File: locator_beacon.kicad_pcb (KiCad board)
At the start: 2 copper layers, 44.2 x 19.9 mm, 37 parts, among them Q1 IRLZ44N, U3 L78L05_SOT89, U5 TL074

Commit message: Add boost IC
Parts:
- removed D1: S1M, Diode_SMD:D_SMA
- removed Q1: IRLZ44N, Package_TO_SOT_SMD:SOT-89-3_Handsoldering
- removed REF**: KiCad-Logo2_5mm_SilkScreen, Symbol:KiCad-Logo2_5mm_SilkScreen
- removed REF**: OSHW-Symbol_6.7x6mm_SilkScreen, Symbol:OSHW-Symbol_6.7x6mm_SilkScreen
- added C3: 4.7u, Capacitor_SMD:C_1206_3216Metric_Pad1.33x1.80mm_HandSolder, F.Cu at (134.6, 77.2)
- added D3: B120-E3, Diode_SMD:D_SMA_Handsoldering, F.Cu at (136.4, 72.9)
- added U4: ~, Package_TO_SOT_SMD:SOT-23-5_HandSoldering, F.Cu at (129.3, 71.1)
- C1: value C_Polarized -> 4.7uF
- C4: value 150u -> 2.2u; footprint Capacitor_THT:CP_Radial_D4.0mm_P1.50mm -> Capacitor_SMD:C_1206_3216Metric_Pad1.33x1.80mm_HandSolder; moved to F.Cu
- C8: moved to F.Cu
- L1: value 22u -> 10u
- R16: value 100k -> 230k
- moved R16 9.98 mm to (139.9, 69.6)
- moved R15 9.93 mm to (134.8, 69.6)
- moved C4 6.41 mm to (125.5, 71.1), turned to 90 degrees
- moved C8 5.62 mm to (140.7, 76.8), turned to 0 degrees
- moved D2 3.42 mm to (137.0, 77.2), turned to -90 degrees
- moved C2 0.97 mm to (119.6, 76.7), turned to 180 degrees
- moved C1 0.16 mm to (158.8, 66.7)
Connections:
- R15 pad 1: /power/Vsense -> Net-(U4-FB)
- R16 pad 1: /power/Vsense -> Net-(U4-FB)
- U1 pad 16: /power/PWMctl -> unconnected-(U1-GP0-Pad16)
- U1 pad 4: /power/Vsense -> unconnected-(U1-GP29-Pad4)
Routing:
- net /power/PWMctl: track 16.6 -> 0.00 mm
- net Net-(U4-FB): track 0.00 -> 8.87 mm
- net GND: track 104.0 -> 110.2 mm
- net /power/Vsense: track 4.91 -> 0.00 mm
- net Net-(D3-A): track 12.1 -> 7.89 mm
- net +BATT: track 17.8 -> 20.2 mm
- net Vdrive: track 48.0 -> 48.6 mm, vias 2 -> 1

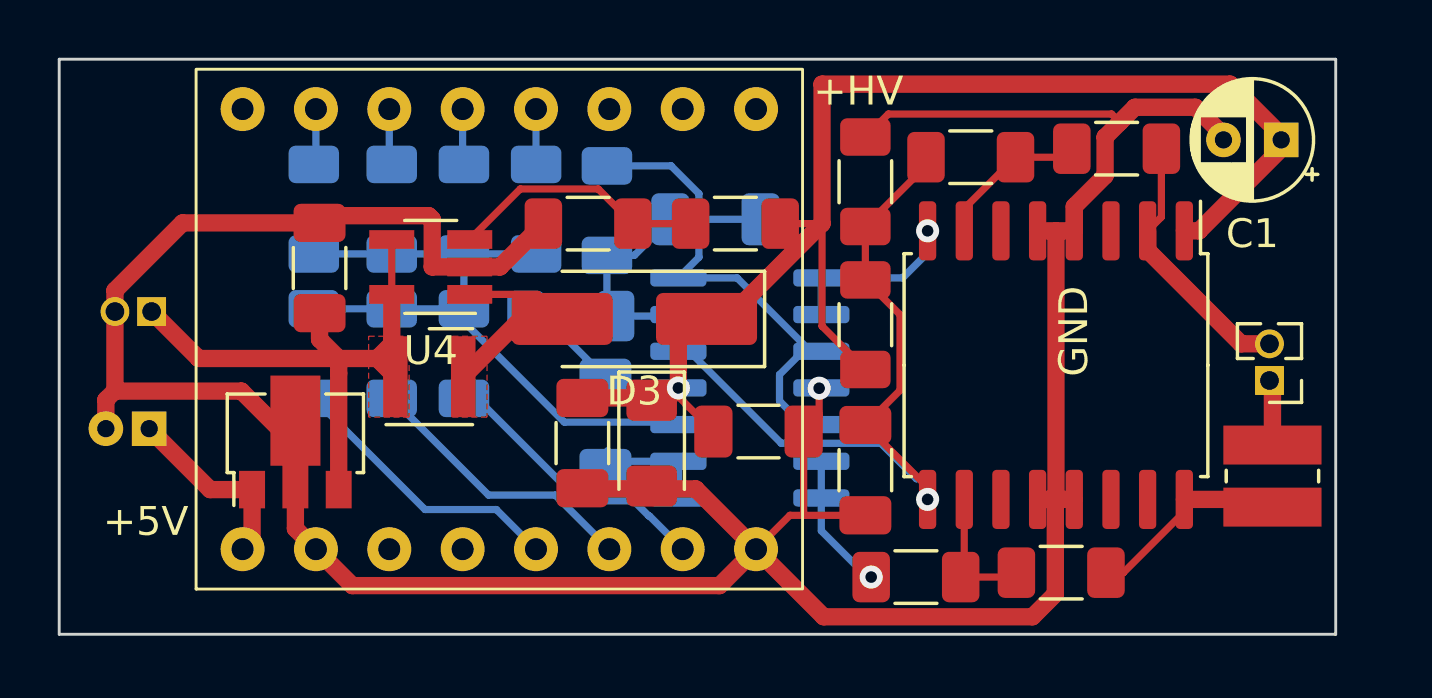
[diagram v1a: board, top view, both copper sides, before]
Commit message: First production prototype
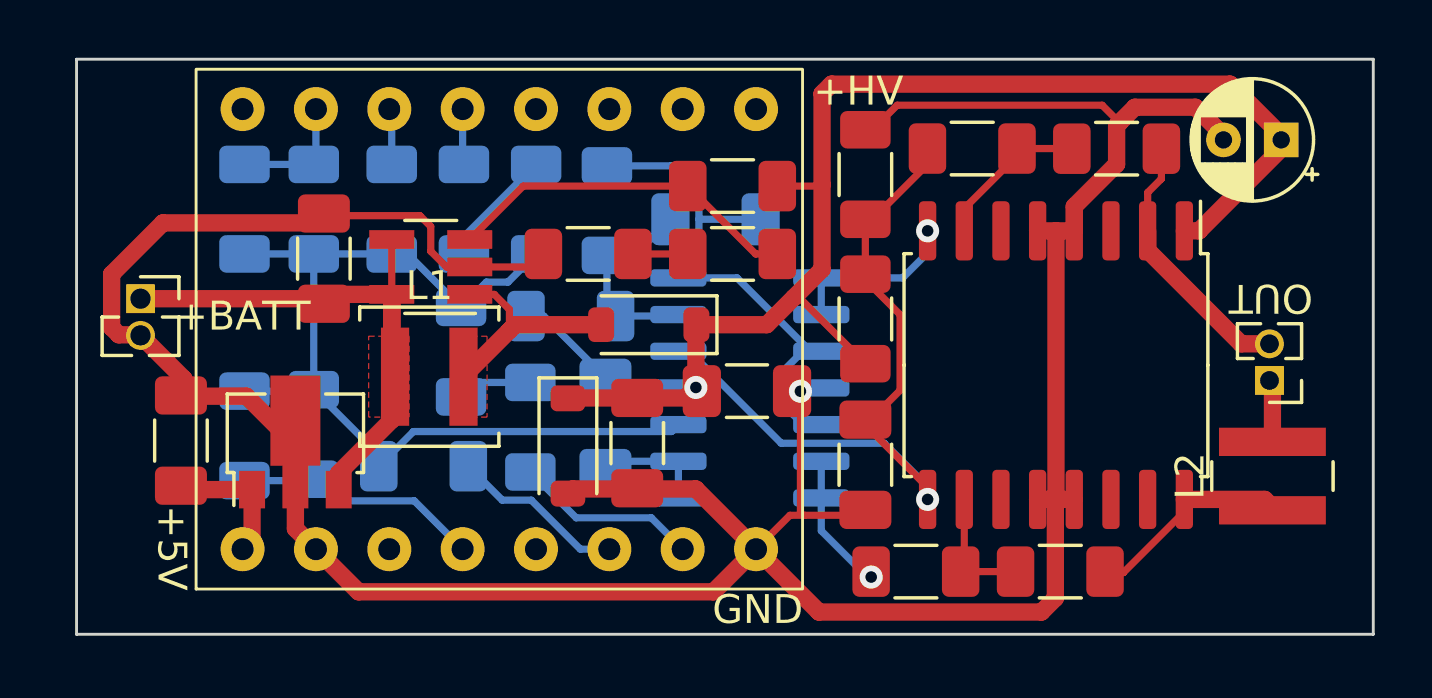
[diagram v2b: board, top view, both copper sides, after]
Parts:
- removed C4: 2.2u, Capacitor_SMD:C_1206_3216Metric_Pad1.33x1.80mm_HandSolder
- added C5: 4.7u, Capacitor_SMD:C_1206_3216Metric_Pad1.33x1.80mm_HandSolder, F.Cu at (120.7, 77.1)
- added R12: 2k, Resistor_SMD:R_1206_3216Metric_Pad1.30x1.75mm_HandSolder, B.Cu at (122.9, 69.1)
- added R13: 16k, Resistor_SMD:R_1206_3216Metric_Pad1.30x1.75mm_HandSolder, B.Cu at (122.9, 77.0)
- added R17: 16k, Resistor_SMD:R_1206_3216Metric_Pad1.30x1.75mm_HandSolder, B.Cu at (130.4, 74.0)
- added R18: 2k, Resistor_SMD:R_1206_3216Metric_Pad1.30x1.75mm_HandSolder, F.Cu at (134.8, 70.7)
- BT1: footprint Connector_PinHeader_1.27mm:PinHeader_1x02_P1.27mm_Vertical -> Connector_PinSocket_1.27mm:PinSocket_1x02_P1.27mm_Vertical; moved to F.Cu
- C1: value 4.7uF -> 4.7u
- C2: value 150u -> 4.7u; footprint Capacitor_THT:CP_Radial_D4.0mm_P1.50mm -> Capacitor_SMD:C_1206_3216Metric_Pad1.33x1.80mm_HandSolder; moved to F.Cu
- C8: value 10n -> 10u
- D2: footprint Diode_SMD:D_1206_3216Metric_Pad1.42x1.75mm_HandSolder -> Diode_SMD:D_SOD-123
- D3: footprint Diode_SMD:D_SMA_Handsoldering -> Diode_SMD:D_SOD-123
- L1: footprint Inductor_SMD_Wurth:L_Wurth_WE-LQSH-3012 -> Inductor_SMD:L_Coilcraft_XAL4030-XXX
- L2: footprint Inductor_SMD:L_Wuerth_MAPI-3020 -> Inductor_SMD:L_Wuerth_MAPI-4030
- R10: value 1k -> 2k
- R11: value 64k -> 16k
- R15: value 10k -> 2k
- R16: value 230k -> 100k
- R20: value 18.8k -> 16k
- R4: value 13.4k -> 16k
- R5: value 32k -> 16k
- R7: value 8k -> 2k
- R8: value 4k -> 2k
- U2: value ~ -> TCA0372
- U4: value ~ -> MIC2288
- moved C2 8.44 mm to (125.7, 70.8), turned to 90 degrees
- moved R15 5.11 mm to (139.8, 70.7)
- moved R5 4.05 mm to (129.1, 78.0), turned to 0 degrees
- moved R11 3.43 mm to (132.8, 76.7)
- moved D2 2.90 mm to (134.1, 77.3)
- moved R6 2.80 mm to (125.3, 76.9)
- moved C3 1.90 mm to (136.5, 77.2)
- moved C8 1.46 mm to (140.3, 75.4)
- moved R16 1.30 mm to (139.8, 68.3)
- moved BT1 0.59 mm to (119.3, 72.2), turned to 0 degrees
- moved D3 0.54 mm to (136.9, 73.1)
- moved R21 0.30 mm to (148.1, 67.0)
- moved R19 0.25 mm to (144.4, 67.9)
- moved R2 0.20 mm to (144.4, 72.9)
- moved R3 0.19 mm to (146.2, 81.7)
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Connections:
- C2 pad 1: +5V -> +BATT
- R11 pad 1: Net-(U5A-+) -> Net-(R11-Pad1)
- R15 pad 2: GND -> Net-(R15-Pad2)
- R6 pad 2: Net-(U1-GP28) -> Net-(U1-GP29)
- R7 pad 1: Net-(U1-GP4) -> Net-(U5A-+)
- R7 pad 2: Net-(U5A-+) -> Net-(R7-Pad2)
- R8 pad 2: Net-(U5A-+) -> Net-(R7-Pad2)
- U1 pad 12: Net-(U1-GP4) -> unconnected-(U1-GP4-Pad12)
- U1 pad 4: unconnected-(U1-GP29-Pad4) -> Net-(U1-GP29)
- U1 pad 5: Net-(U1-GP28) -> unconnected-(U1-GP28-Pad5)
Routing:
- net Net-(U1-GP28): track 9.86 -> 0.00 mm
- net Net-(U5A-+): track 24.1 -> 33.3 mm
- net Net-(U1-GP29): track 0.00 -> 8.58 mm
- net Net-(R7-Pad2): track 0.00 -> 4.14 mm
- net Vdrive: track 48.6 -> 44.8 mm
- net Net-(U1-GP27): track 9.70 -> 6.07 mm
- net Net-(U4-FB): track 8.87 -> 12.4 mm
- net Net-(U1-GP26): track 9.74 -> 6.38 mm
- net Net-(R11-Pad1): track 0.00 -> 2.61 mm
- net Net-(U1-GP1): track 2.05 -> 4.34 mm
- net +5V: track 6.64 -> 4.61 mm
- net Net-(U1-GP4): track 1.92 -> 0.00 mm
- net Net-(R15-Pad2): track 0.00 -> 1.90 mm
- net +BATT: track 20.2 -> 21.8 mm
- net GND: track 110.2 -> 109.6 mm
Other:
- board size 44.2 x 19.9 mm -> 44.9 x 19.9 mm
- board text added: "DAC"
- board text added: "OUT"
- board text added: "SHAPER"

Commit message: Prod 1a
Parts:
- BT1: footprint Connector_PinSocket_1.27mm:PinSocket_1x02_P1.27mm_Vertical -> Connector_PinHeader_2.54mm:PinHeader_1x02_P2.54mm_Vertical
- OUT1: footprint Connector_PinHeader_1.27mm:PinHeader_1x02_P1.27mm_Vertical -> Connector_PinSocket_2.54mm:PinSocket_1x02_P2.54mm_Vertical
- U3: footprint Package_TO_SOT_SMD:SOT-89-3 -> Package_TO_SOT_SMD:TO-252-2
- moved R19 9.89 mm to (143.1, 77.7), turned to 0 degrees
- moved BT1 7.21 mm to (119.3, 79.4)
- moved C5 6.70 mm to (127.4, 77.2), turned to -90 degrees
- moved U3 5.81 mm to (122.6, 71.4)
- moved C6 4.60 mm to (144.4, 73.3)
- moved R2 4.55 mm to (144.4, 68.3), turned to 90 degrees
- moved U4 2.53 mm to (131.3, 69.5)
- moved C2 2.25 mm to (127.3, 69.3)
- moved R18 1.80 mm to (136.1, 69.4), turned to -90 degrees
- moved L1 1.70 mm to (130.9, 74.5)
- moved D2 0.40 mm to (134.5, 77.3)
- moved C3 0.35 mm to (136.8, 77.2)
- moved C8 0.35 mm to (140.7, 75.4)
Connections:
- U3 pad 1: +5V -> +BATT
- U3 pad 3: +BATT -> +5V
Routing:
- net GND: track 109.6 -> 95.2 mm
- net +5V: track 4.61 -> 7.86 mm
- net Net-(U4-FB): track 12.4 -> 9.93 mm
- net Vdrive: track 44.8 -> 42.5 mm
- net /VGND: track 25.6 -> 26.9 mm
- net Net-(D3-A): track 7.99 -> 7.05 mm
- net Net-(OUT1-Pad2): track 8.98 -> 8.46 mm
- removed copper zone on F.Cu, net +BATT
- removed copper zone on F.Cu, net Net-(D3-A)
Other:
- board text added: "BOOST"

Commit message: Forgot to save
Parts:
- removed C8: 10u, Capacitor_SMD:C_1206_3216Metric_Pad1.33x1.80mm_HandSolder
- removed D2: 30V, Diode_SMD:D_SOD-123
- removed R10, R7, R8, R9: 2k, Resistor_SMD:R_1206_3216Metric_Pad1.30x1.75mm_HandSolder
- removed R11, R13, R17, R20, R4, R5, R6: 16k, Resistor_SMD:R_1206_3216Metric_Pad1.30x1.75mm_HandSolder
- removed U3: L78L05_SOT89, Package_TO_SOT_SMD:TO-252-2
- removed U5: TL074, Package_SO:SOIC-14_3.9x8.7mm_P1.27mm
- added C4: 4.7u, Capacitor_SMD:C_1206_3216Metric_Pad1.33x1.80mm_HandSolder, F.Cu at (126.3, 54.7)
- added L3: 4.7u, Inductor_SMD:L_Coilcraft_XAL4030-XXX, F.Cu at (126.2, 59.4)
- added U6: XC9140, Package_SO:TSOP-5_1.65x3.05mm_P0.95mm, F.Cu at (131.5, 58.7)
- C5: value 4.7u -> 10u
- C6, R1, R14, R19, R2, R21, R3, U2: moved to B.Cu
- C7: value 2.2n -> 4.7n
- moved R1 16.3 mm to (146.9, 65.9)
- moved L2 16.2 mm to (174.7, 76.8)
- moved R14 16.2 mm to (141.2, 78.0)
- moved R21 11.1 mm to (139.7, 74.2), turned to -90 degrees
- moved R12 9.48 mm to (132.3, 69.8)
- moved R3 9.42 mm to (142.3, 73.0), turned to -90 degrees
- moved R19 8.26 mm to (134.9, 76.3), turned to 90 degrees
- moved C6 7.71 mm to (137.3, 76.3)
- moved R2 7.34 mm to (137.2, 69.8)
- moved C7 4.43 mm to (134.8, 69.8), turned to 90 degrees
- moved C9 2.90 mm to (132.5, 76.4)
- moved OUT1 2.86 mm to (157.9, 72.2), turned to 0 degrees
- moved U2 2.26 mm to (149.2, 73.2), turned to 90 degrees
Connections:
- C7 pad 1: Net-(U5B--) -> Net-(C7-Pad1)
- C7 pad 2: Net-(U5C-+) -> Net-(U2A-+)
- C9 pad 1: Net-(C9-Pad1) -> Net-(C7-Pad1)
- C9 pad 2: Net-(U5A--) -> GND
- R12 pad 2: Net-(U5A-+) -> Net-(C7-Pad1)
- R3 pad 2: Net-(U5D--) -> Net-(U2A-+)
- U1 pad 13: Net-(U1-GP3) -> unconnected-(U1-GP3-Pad13)
- U1 pad 14: Net-(U1-GP2) -> unconnected-(U1-GP2-Pad14)
- U1 pad 3: +3.3V -> unconnected-(U1-3V3-Pad3)
- U1 pad 4: Net-(U1-GP29) -> unconnected-(U1-GP29-Pad4)
- U1 pad 6: Net-(U1-GP27) -> unconnected-(U1-GP27-Pad6)
- U1 pad 7: Net-(U1-GP26) -> unconnected-(U1-GP26-Pad7)
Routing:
- net Vdrive: track 42.5 -> 0.00 mm, vias 1 -> 0
- net GND: track 95.2 -> 55.2 mm, vias 1 -> 0
- net Net-(U5A-+): track 33.3 -> 0.00 mm
- net Net-(U5C-+): track 19.0 -> 0.00 mm
- net /VGND: track 26.9 -> 16.4 mm, vias 1 -> 0
- net Net-(OUT1-Pad2): track 8.46 -> 18.1 mm
- net Net-(U1-GP29): track 8.58 -> 0.00 mm
- net Net-(U2A--): track 5.06 -> 13.4 mm
- net Net-(U5B--): track 7.14 -> 0.00 mm
- net Net-(U1-GP26): track 6.38 -> 0.00 mm
- net Net-(U1-GP27): track 6.07 -> 0.00 mm
- net Net-(C7-Pad1): track 0.00 -> 5.93 mm
- net Net-(U2B--): track 4.27 -> 9.91 mm
- net Net-(U5D--): track 4.84 -> 0.00 mm, vias 1 -> 0
- net Net-(U1-GP1): track 4.34 -> 0.00 mm
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
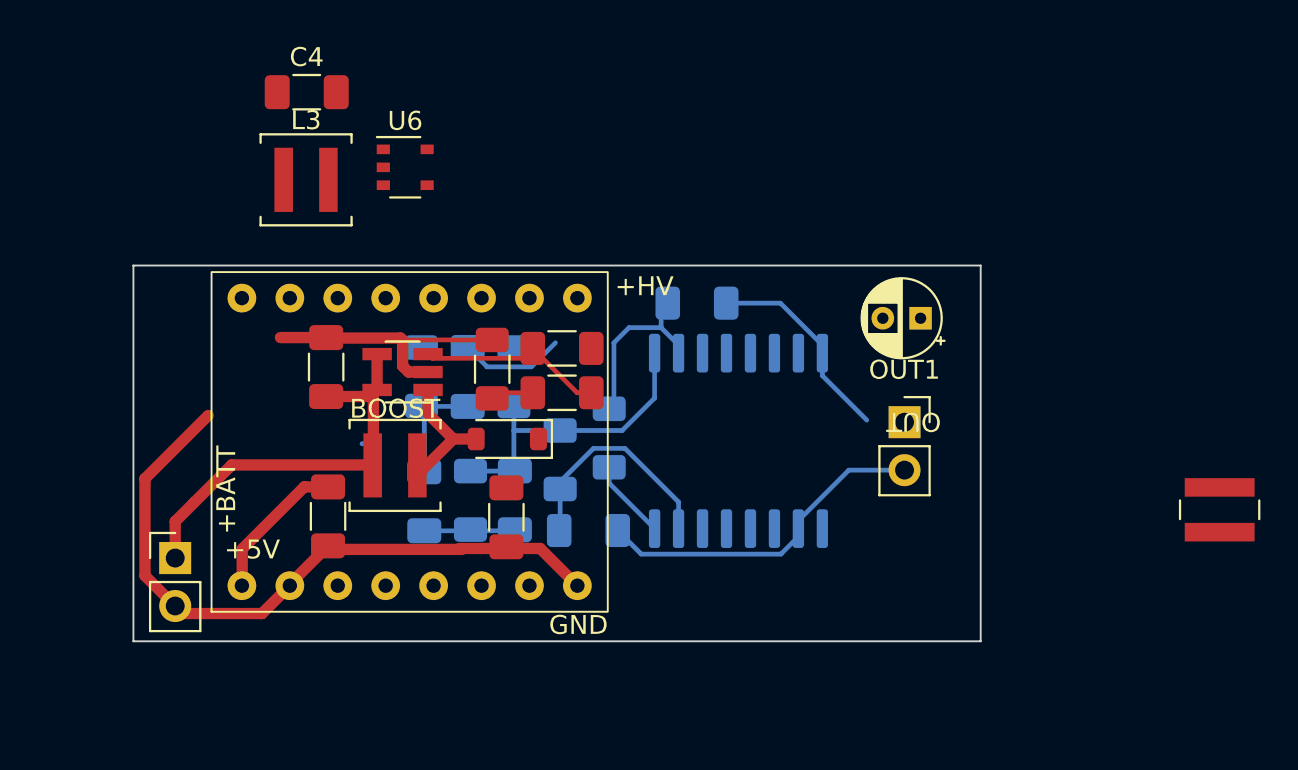
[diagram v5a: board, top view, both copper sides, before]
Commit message: Basic Class D amp
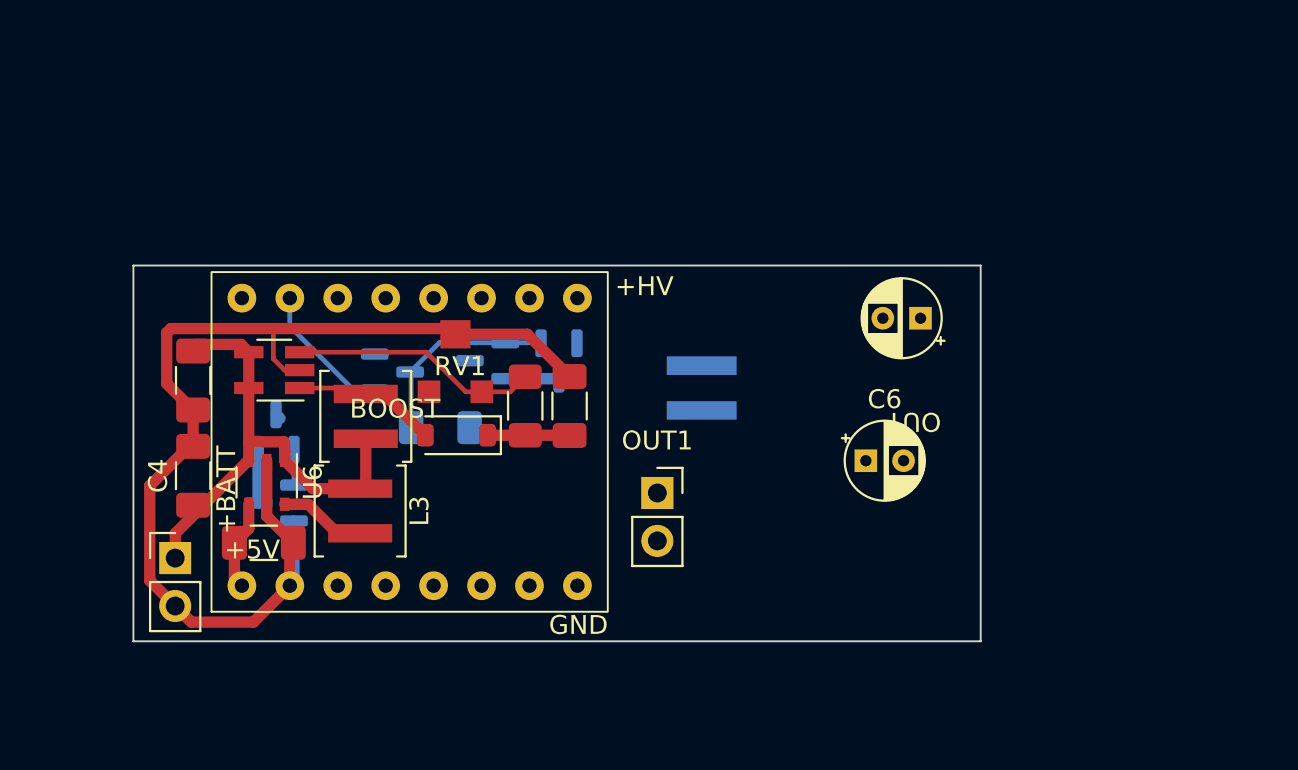
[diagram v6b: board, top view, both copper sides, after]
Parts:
- removed C7, C9: 4.7n, Capacitor_SMD:C_1206_3216Metric_Pad1.33x1.80mm_HandSolder
- removed R12, R15, R18: 2k, Resistor_SMD:R_1206_3216Metric_Pad1.30x1.75mm_HandSolder
- removed R14, R19, R2: 100k, Resistor_SMD:R_1206_3216Metric_Pad1.30x1.75mm_HandSolder
- removed R21: 6.5k, Resistor_SMD:R_1206_3216Metric_Pad1.30x1.75mm_HandSolder
- removed R3: 6k, Resistor_SMD:R_1206_3216Metric_Pad1.30x1.75mm_HandSolder
- removed U2: TCA0372, Package_SO:SOIC-16W_7.5x10.3mm_P1.27mm
- added Q1: DMG3406L, Package_TO_SOT_SMD:SOT-23, B.Cu at (124.7, 76.5)
- added Q2: DMP3099, Package_TO_SOT_SMD:SOT-23, B.Cu at (124.6, 72.7)
- added Q3: DMP3099, Package_TO_SOT_SMD:SOT-23, B.Cu at (135.8, 69.0)
- added Q4: DMG3406L, Package_TO_SOT_SMD:SOT-23, B.Cu at (139.6, 69.0)
- added Q5: DMG3406L, Package_TO_SOT_SMD:SOT-23, B.Cu at (130.8, 69.5)
- added RV1: R_Potentiometer_Trim, custom:trimpot, F.Cu at (134.2, 69.0)
- C6: value 10u -> 4.7u; footprint Capacitor_SMD:C_1206_3216Metric_Pad1.33x1.80mm_HandSolder -> Capacitor_THT:CP_Radial_D4.0mm_P2.00mm; moved to F.Cu
- L2: moved to B.Cu
- moved L2 28.2 mm to (147.2, 70.4), turned to -90 degrees
- moved C4 21.2 mm to (120.2, 75.0), turned to 90 degrees
- moved C6 18.7 mm to (155.9, 74.2), turned to 0 degrees
- moved U6 18.2 mm to (124.2, 75.4), turned to -90 degrees
- moved L3 17.8 mm to (129.1, 76.9), turned to -90 degrees
- moved R1 15.1 mm to (133.3, 72.5)
- moved OUT1 13.6 mm to (144.8, 76.0)
- moved C2 7.09 mm to (120.2, 70.0), turned to -90 degrees
- moved U4 6.80 mm to (124.5, 69.5)
- moved C3 6.78 mm to (140.2, 71.3), turned to 90 degrees
- moved C5 3.68 mm to (124.0, 78.6), turned to 0 degrees
- moved R16 3.62 mm to (137.8, 71.3), turned to -90 degrees
- moved L1 3.03 mm to (129.4, 71.9), turned to 90 degrees
- moved D3 2.71 mm to (134.2, 72.9)
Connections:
- C6 pad 1: /VGND -> Vdrive
- L2 pad 1: Net-(L2-Pad1) -> /OUT_P
- OUT1 pad 2: Net-(OUT1-Pad2) -> /OUT_M
- R1 pad 1: Net-(L2-Pad1) -> Vdrive
- R1 pad 2: Net-(U2B--) -> /SIG_M
- U1 pad 15: Net-(U1-GP1) -> /SIG_P
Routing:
- net Net-(OUT1-Pad2): track 18.1 -> 0.00 mm
- net /VGND: track 16.4 -> 0.00 mm
- net Net-(U2A--): track 13.4 -> 0.00 mm
- net Net-(L2-Pad1): track 11.0 -> 0.00 mm
- net /SIG_M: track 0.00 -> 10.6 mm
- net Net-(U2B--): track 9.91 -> 0.00 mm
- net Net-(U2A-+): track 9.85 -> 0.00 mm
- net /SIG_P: track 0.00 -> 9.26 mm
- net Net-(C7-Pad1): track 5.93 -> 0.00 mm
- net GND: track 55.2 -> 60.7 mm
- net Vdrive: track 0.00 -> 4.66 mm
- net Net-(U6-L_{x}): track 0.00 -> 4.64 mm
- net +BATT: track 21.9 -> 25.9 mm
- net Net-(U4-FB): track 9.93 -> 13.2 mm
- net +5V: track 7.86 -> 4.79 mm
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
